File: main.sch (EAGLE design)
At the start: 83 parts, among them Q1 5.8A/30V/35mΩ, Q2 5.8A/30V/35mΩ, Q3 2.5A/30V/105mΩ, U1 BQ24133_RGY_24, U2 SN65HVD32_D_8

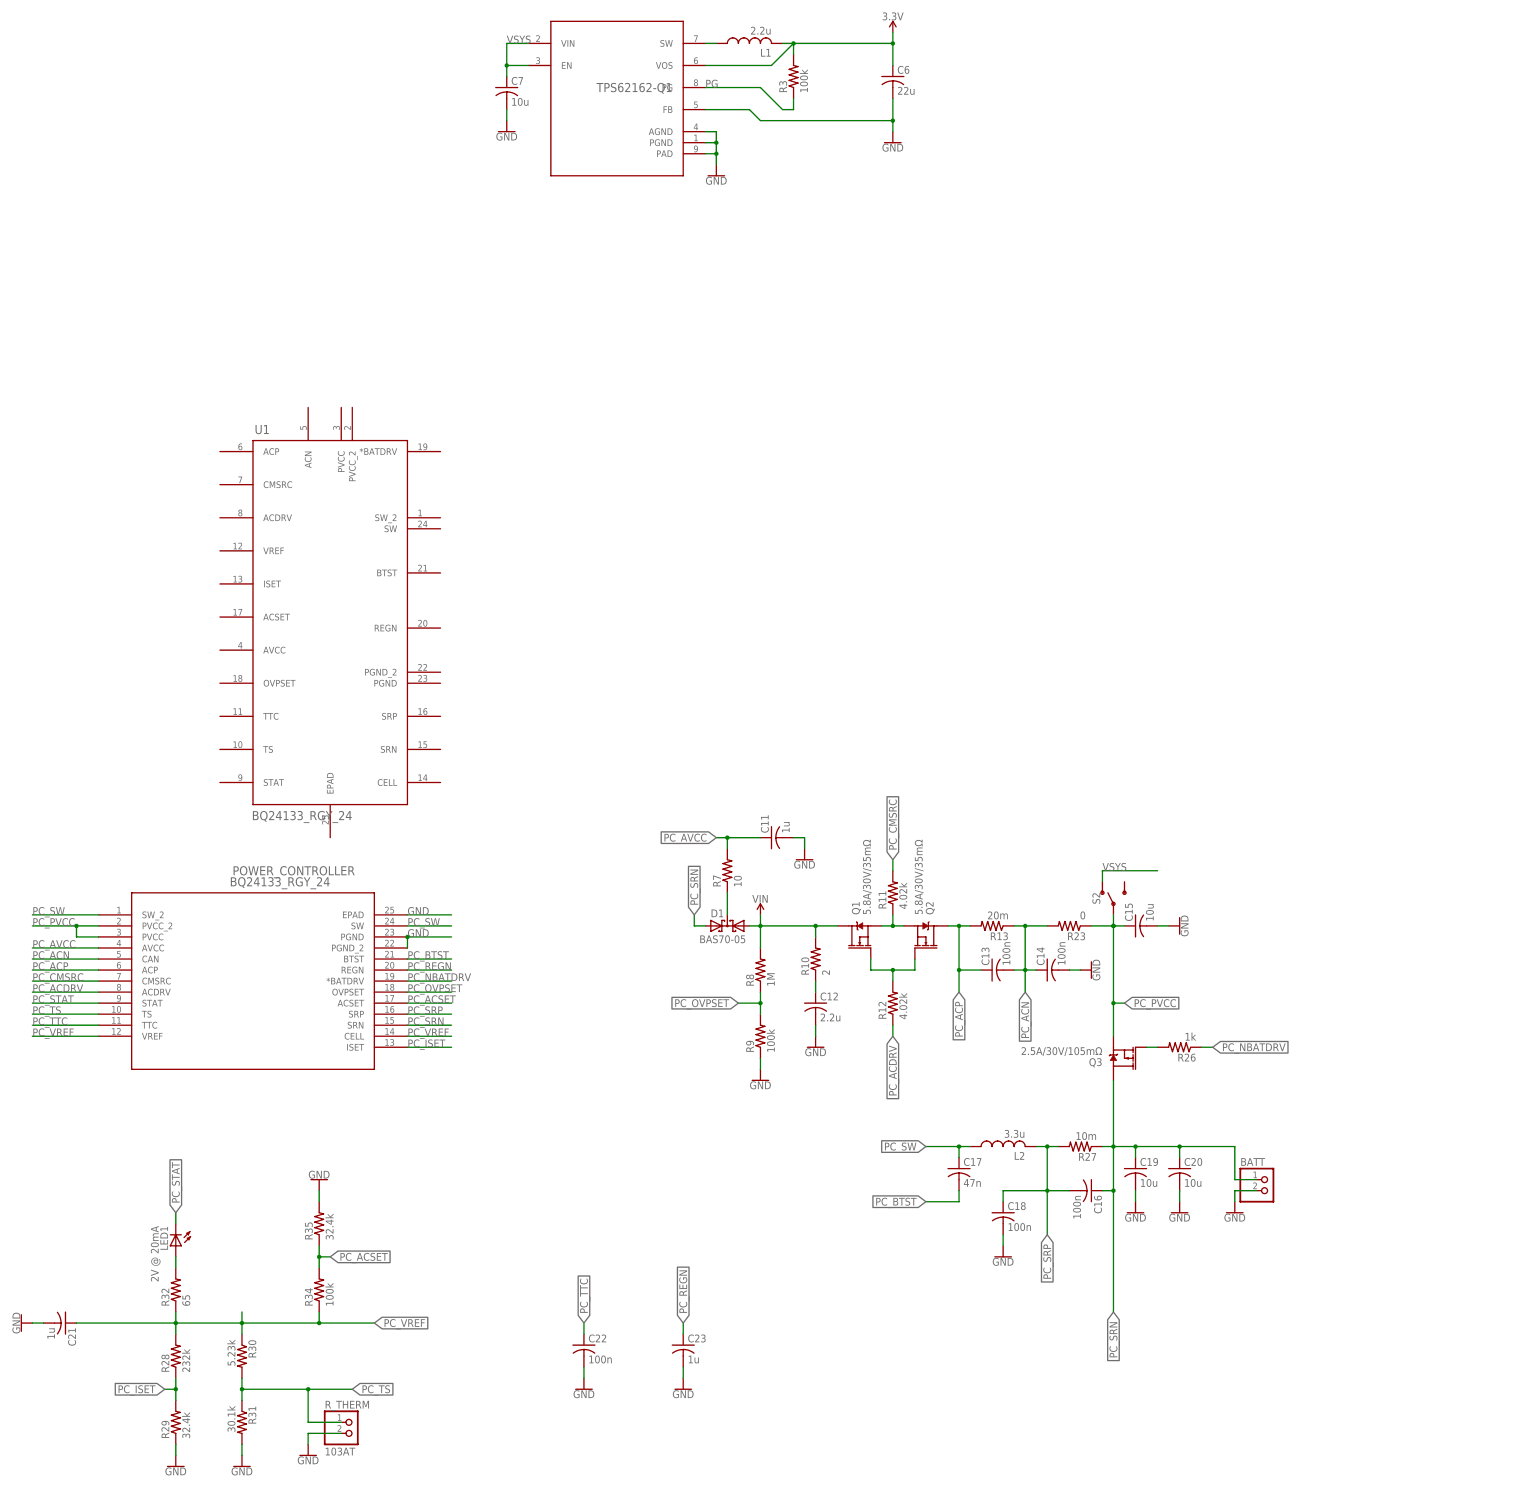
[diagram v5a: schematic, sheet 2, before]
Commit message: Updated Power Schematics
Attatched to new model, better represents power controller datasheet.
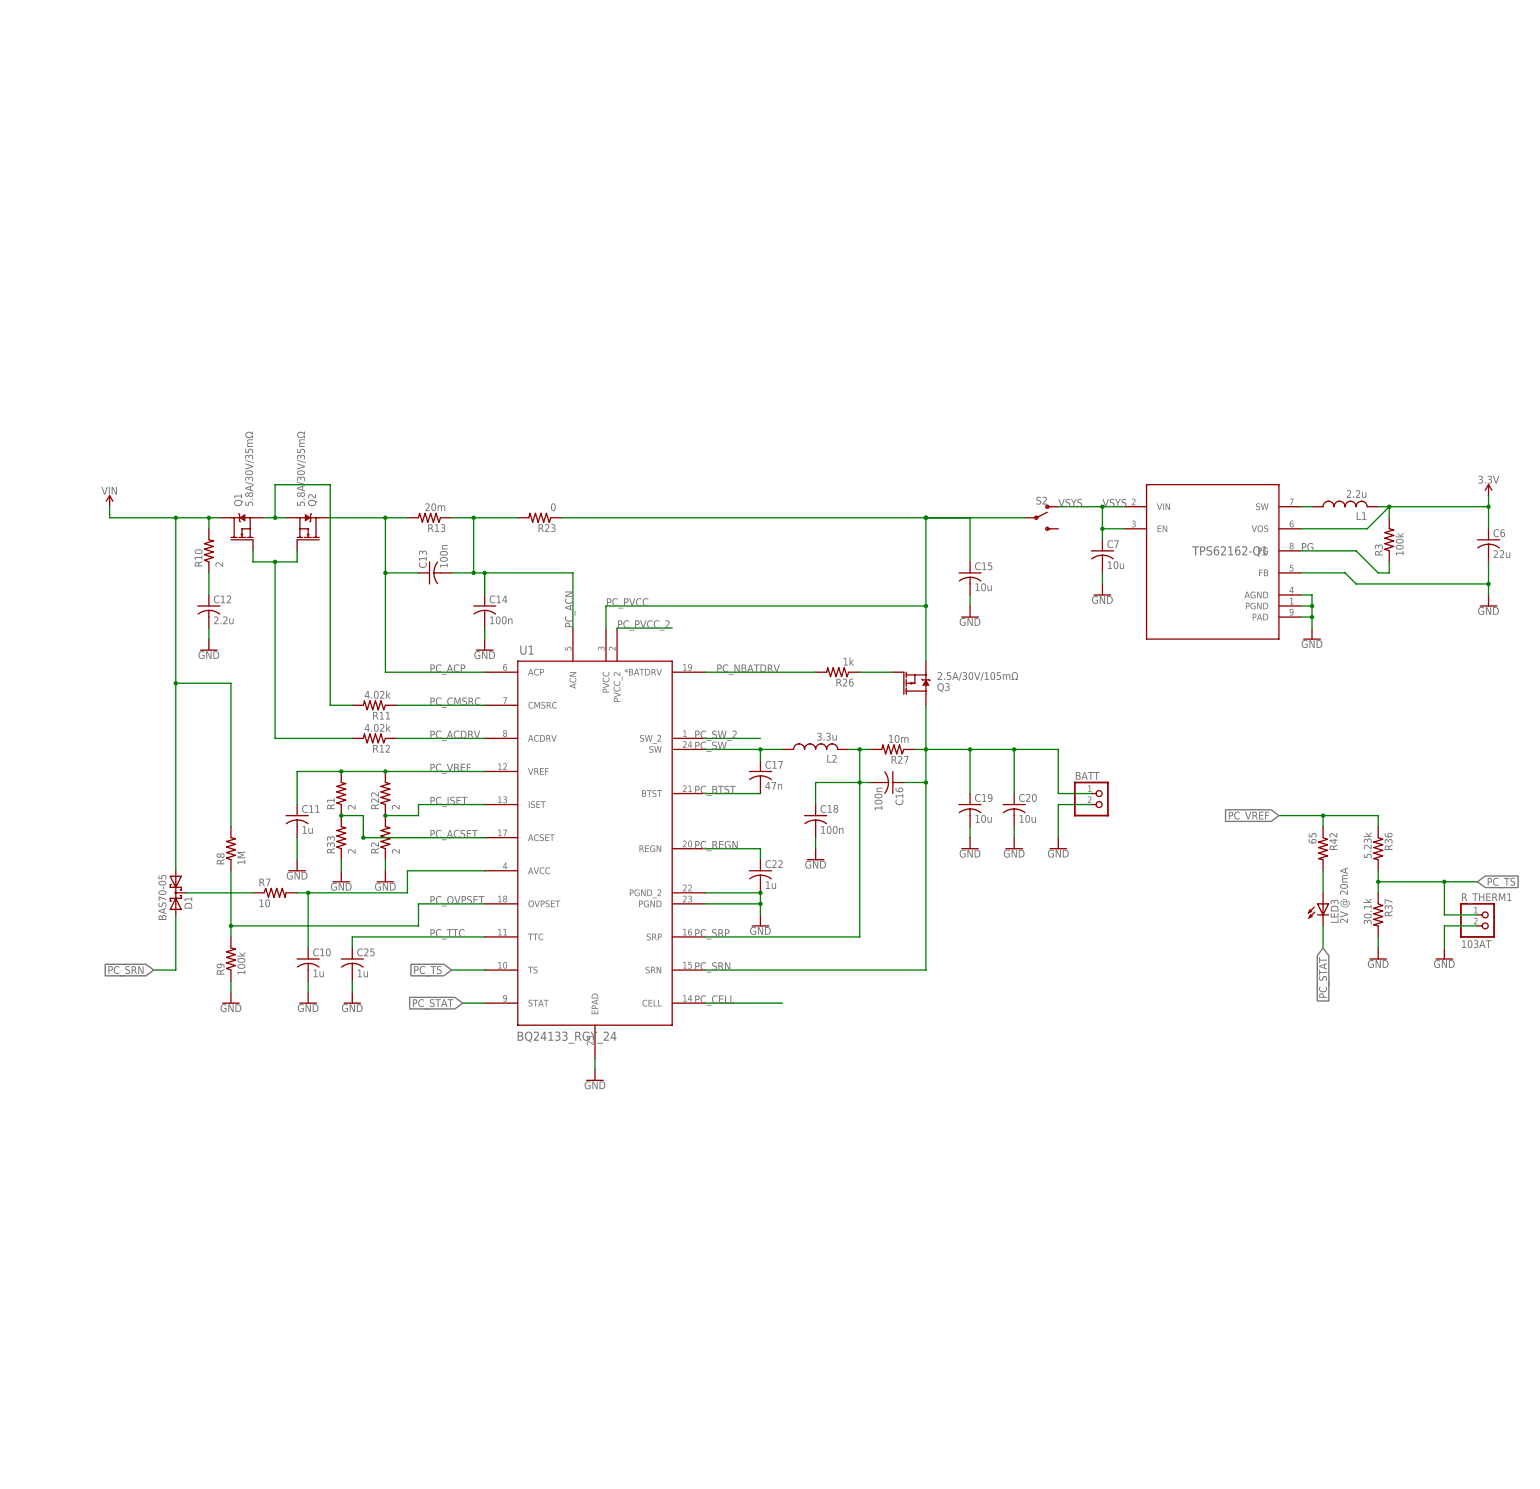
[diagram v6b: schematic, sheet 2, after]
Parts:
- removed C21, C23: 1u, resistor:C-USC0603
- removed LED1: 2V @ 20mA, adafruit:LEDCHIPLED_0603
- removed POWER_CONTROLLER: BQ24133_RGY_24, BQ24133:BQ24133_RGY_24
- removed R28: 232k, resistor:R-US_R0603
- removed R29, R35: 32.4k, resistor:R-US_R0603
- removed R30: 5.23k, resistor:R-US_R0603
- removed R31: 30.1k, resistor:R-US_R0603
- removed R32: 65, resistor:R-US_R0603
- removed R34: 100k, resistor:R-US_R0603
- removed R_THERM: 103AT, pinhead:PINHD-1X2
- added C10, C25: 1u, rcl:C-USC1206
- added LED3: 2V @ 20mA, adafruit:LEDCHIPLED_0603
- added R1, R2, R22, R33: 2, resistor:R-US_R0603
- added R36: 5.23k, resistor:R-US_R0603
- added R37: 30.1k, resistor:R-US_R0603
- added R42: 65, resistor:R-US_R0603
- added R_THERM1: 103AT, pinhead:PINHD-1X2
- C22: value 100n -> 1u
- Q1: SPICEPREFIX (none) -> Q
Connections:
- removed net N$20: LED1.A, R32.2
- removed net PC_AVCC: C11.1, POWER_CONTROLLER.AVCC, R7.2
- new net N$10: Q3.G, R26.1
- new net N$21: C25.2
- new net N$22: U1.TS
- new net N$23: LED3.A, R42.2
- new net N$24: U1.STAT
- new net PC_CELL: U1.CELL
- new net PC_PVCC_2: U1.PVCC_2
- new net PC_SW_2: U1.SW_2
- new net PC_VREF1: R36.1, R42.1
- net GND: now also C10.2, R2.1, R33.1, R37.2, R_THERM1.2, U1.EPAD, U1.PGND, U1.PGND_2; no longer C21.2, C23.2, POWER_CONTROLLER.EPAD, POWER_CONTROLLER.PGND, POWER_CONTROLLER.PGND_2, R29.1, R31.2, R35.2, R_THERM.2
- net N$16: now also R11.2; no longer R11.1
- net N$19: now also C10.1, R7.2, U1.AVCC; no longer Q3.G, R26.2
- net PC_ACDRV: now also U1.ACDRV; no longer POWER_CONTROLLER.ACDRV
- net PC_ACN: now also U1.ACN; no longer POWER_CONTROLLER.CAN
- net PC_ACP: now also U1.ACP; no longer POWER_CONTROLLER.ACP
- net PC_ACSET: now also R1.1, R33.2, U1.ACSET; no longer POWER_CONTROLLER.ACSET, R34.2, R35.1
- net PC_BTST: now also U1.BTST; no longer POWER_CONTROLLER.BTST
- net PC_CMSRC: now also R11.1, U1.CMSRC; no longer POWER_CONTROLLER.CMSRC, R11.2
- net PC_ISET: now also R2.2, R22.1, U1.ISET; no longer POWER_CONTROLLER.ISET, R28.1, R29.2
- net PC_NBATDRV: now also R26.2, U1.*BATDRV; no longer POWER_CONTROLLER.*BATDRV, R26.1
- net PC_OVPSET: now also U1.OVPSET; no longer POWER_CONTROLLER.OVPSET
- net PC_PVCC: now also U1.PVCC; no longer POWER_CONTROLLER.PVCC, POWER_CONTROLLER.PVCC_2
- net PC_REGN: now also C22.1, U1.REGN; no longer C23.1, POWER_CONTROLLER.REGN
- net PC_SRN: now also U1.SRN; no longer POWER_CONTROLLER.SRN
- net PC_SRP: now also U1.SRP; no longer POWER_CONTROLLER.SRP
- net PC_STAT: now also LED3.C; no longer LED1.C, POWER_CONTROLLER.STAT
- net PC_SW: now also U1.SW; no longer POWER_CONTROLLER.SW, POWER_CONTROLLER.SW_2
- net PC_TS: now also R36.2, R37.1, R_THERM1.1; no longer POWER_CONTROLLER.TS, R30.2, R31.1, R_THERM.1
- net PC_TTC: now also C25.1, U1.TTC; no longer C22.1, POWER_CONTROLLER.TTC
- net PC_VREF: now also C11.1, R1.2, R22.2, U1.VREF; no longer C21.1, POWER_CONTROLLER.CELL, POWER_CONTROLLER.VREF, R28.2, R30.1, R32.1, R34.1
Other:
- moved on the sheet: BATT, C11, C12, C13, C14, C15, C16, C17, C18, C19, C20, C22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

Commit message: Seperated AGND and PGND, set a few current limiting pin configs, misc schematic changes
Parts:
- removed C14: 100n, rcl:C-USC1206
- added CIN: 2.2u, rcl:C-USC1206
- added RIN: 2, resistor:R-US_R0603
- C11: value 1u -> 100n; device rcl:C-USC1206 -> resistor:C-USC0603
- C12: value 2.2u -> 100n
- C13: value 100n -> 1u; device resistor:C-USC0603 -> rcl:C-USC1206
- R1: value 2 -> 100k
- R10: value 2 -> 0
- R2: value 2 -> 36.6k
- R22: value 2 -> 232k
- R33: value 2 -> 153.9k
- renumbered R13 to RAC, R27 to RSR, R_THERM1 to RT
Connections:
- removed net N$21: C25.2
- removed net N$29: LED2.A, R41.2
- new net AGND: C10.2, C12.2, C13.2, C18.2, C25.2, R10.2, R2.1, R33.1, R37.2, R9.1, RT.2, U1.EPAD, VCHG.2
- new net N$20: LED2.C, R41.2
- net 3.3V: now also LED2.A
- net GND: now also CIN.2, R10.1; no longer C10.2, C11.2, C12.2, C14.2, C18.2, LED2.C, R2.1, R33.1, R37.2, R9.1, RT.2, U1.EPAD, VCHG.2
- net N$15: now also CIN.1, RIN.1; no longer C12.1, R10.1
- net PC_ACN: now also C11.2, C12.1; no longer C13.2, C14.1
- net PC_ACP: now also C11.1; no longer C13.1
- net PC_VREF: now also C13.1; no longer C11.1
- net VIN: now also RIN.2; no longer R10.2
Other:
- note added: "I calculated Irip = 0.54656A, assuming battery voltage is 11.1V, I believe data sheet max Irip occurs when Vout/Vin is closest to 0.5"
- note added: "Note: (Inductor Saturation current) >= (Charge current) + (ripple current)/2"
- note added: "Note: Chose 15C, 2.25A charge rate limit. Bat is 11.1V 150mAh 35C rated, but don't want to push it. So Viset should be 450mV"
- note added: "Note: Ethernet core current limit is about 300mA, we will be using 2 both ways so 600 mA, so I set current_adapter limit to 500mA"
- note added: "Note: Planning on VIN being 15VDC"
- note added: "Note: These are probably the Cout that ds refers to."
- note added: "This means that Vacset = 2.0V"
- moved on the sheet: C11, C12, C13, LED2, R10, R23

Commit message: Just combined accidental "branches"
Includes last commit and some layout progress.

Co-Authored-By: ohorondi <ohorondi@users.noreply.github.com>
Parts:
- removed CIN: 2.2u, rcl:C-USC1206
- removed RIN: 2, resistor:R-US_R0603
- added C14, C21: 100n, rcl:C-USC1206
- added R28: 0, resistor:R-US_R0603
- C11: value 100n -> 1u; device resistor:C-USC0603 -> rcl:C-USC1206
- C12: value 100n -> 2.2u
- C13: value 1u -> 100n; device rcl:C-USC1206 -> resistor:C-USC0603
- R10: value 0 -> 2
- renumbered RAC to R13, RSR to R27, RT to R_THERM1
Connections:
- net N$19 renamed PC_AVCC
- net N$7 renamed SW
- removed net N$20: LED2.C, R41.2
- removed net N$22: U1.TS
- removed net N$24: U1.STAT
- removed net PC_VREF1: R36.1, R42.1
- new net FB: C6.2, TPS62162-Q1.FB
- new net N$29: LED2.A, R41.2
- new net N$7: D1.A1, Q1.D, R10.2, R8.2
- new net VOS: C6.1, L1.2, R3.2, TPS62162-Q1.VOS
- net 3.3V: no longer C6.1, L1.2, LED2.A, R3.2, TPS62162-Q1.VOS
- net AGND: now also C11.2, C14.2, C21.2, R28.2; no longer C12.2, C13.2, R10.2
- net GND: now also C12.2, LED2.C, R28.1; no longer C6.2, CIN.2, R10.1, TPS62162-Q1.FB
- net N$15: now also C12.1, R10.1; no longer CIN.1, RIN.1
- net PC_ACN: now also C13.2, C14.1; no longer C11.2, C12.1
- net PC_ACP: now also C13.1; no longer C11.1
- net PC_SRN: now also C21.1
- net PC_STAT: now also U1.STAT
- net PC_TS: now also U1.TS
- net PC_VREF: now also C11.1, R36.1, R42.1; no longer C13.1
- net VIN: no longer D1.A1, Q1.D, R8.2, RIN.2
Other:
- note removed: "Note: Planning on VIN being 15VDC"
- moved on the sheet: C11, C12, C13, C16, C18, C6, L1, LED2, Q3, R10, R23, R3
